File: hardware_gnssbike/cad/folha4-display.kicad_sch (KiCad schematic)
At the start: 15 parts, among them J401 Hirose FH12-10S-0.5SH(55), J402 HCTL HC-FPC-05-10-5RLTAG, Q401 DMG1012T-7

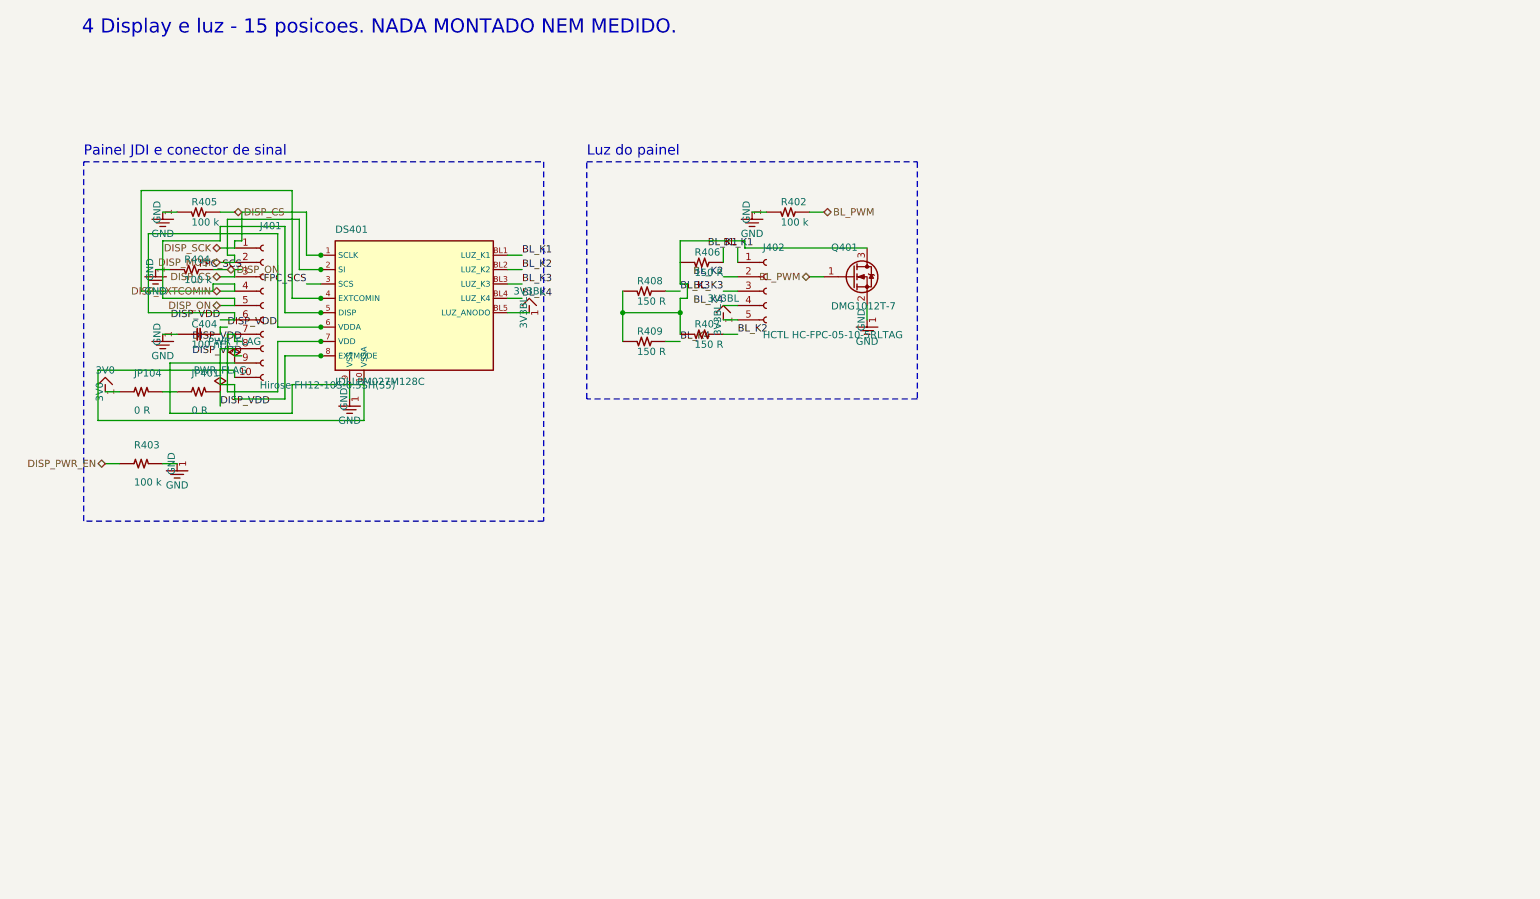
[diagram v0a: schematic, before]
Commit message: feat(hardware): spread the schematic so references, values and labels stay apart
The owner asked for the block-drawn schematic to be readable: designators
and labels were printing over each other. Power symbols now hide the pin
number and name (each printed a "1" and the rail's name twice) and point
away from their pin, lying along the line of a side pin with the name on
that line; the decoupling shelf is a row of stood-up capacitors per rail
with one wire along the tops and one symbol per row, test points standing
too; references and values sit to the right of a standing part and between
the neighbouring lines of a lying one, and block titles, part texts and
symbol names are obstacles for the router and for symbol and label
placement. Pull-ups and pull-downs of a labelled line stand past the label,
and off the corridor when the line goes on to another anchor; the labels'
room is reserved before the members are placed; the FPC connector is
mirrored to face the panel and aligned with it, its board-side wire
continuing from the label point, with the two nets of a pass-through pin
allowed to share cells; the two cells in front of every pin belong to its
net; DISP_VDD is drawn as a rail; blocks are packed by height and sheet 1
fits an A3.

The library symbol now always holds the base drawing and the instance
carries the rotation and mirror. The generator used to write the library
already flipped and the (mirror ...) token as well, applying the transform
twice, and the earlier "measurement" of (mirror x) was inverted by that.
Measured again on minimal files: (mirror y) swaps left for right, an
instance at 90 sends the left pin to the bottom, and KiCad transforms the
field justification along with the instance.

check_sch.py passes: the netlist equals nets.py pin by pin, no new ERC
error, no wire over a component. Eight nets are closed by labels where the
maze found no path inside the block, and the solar harvester and the left
of the gauge remain crowded; SCH_DEBUG=1 exp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
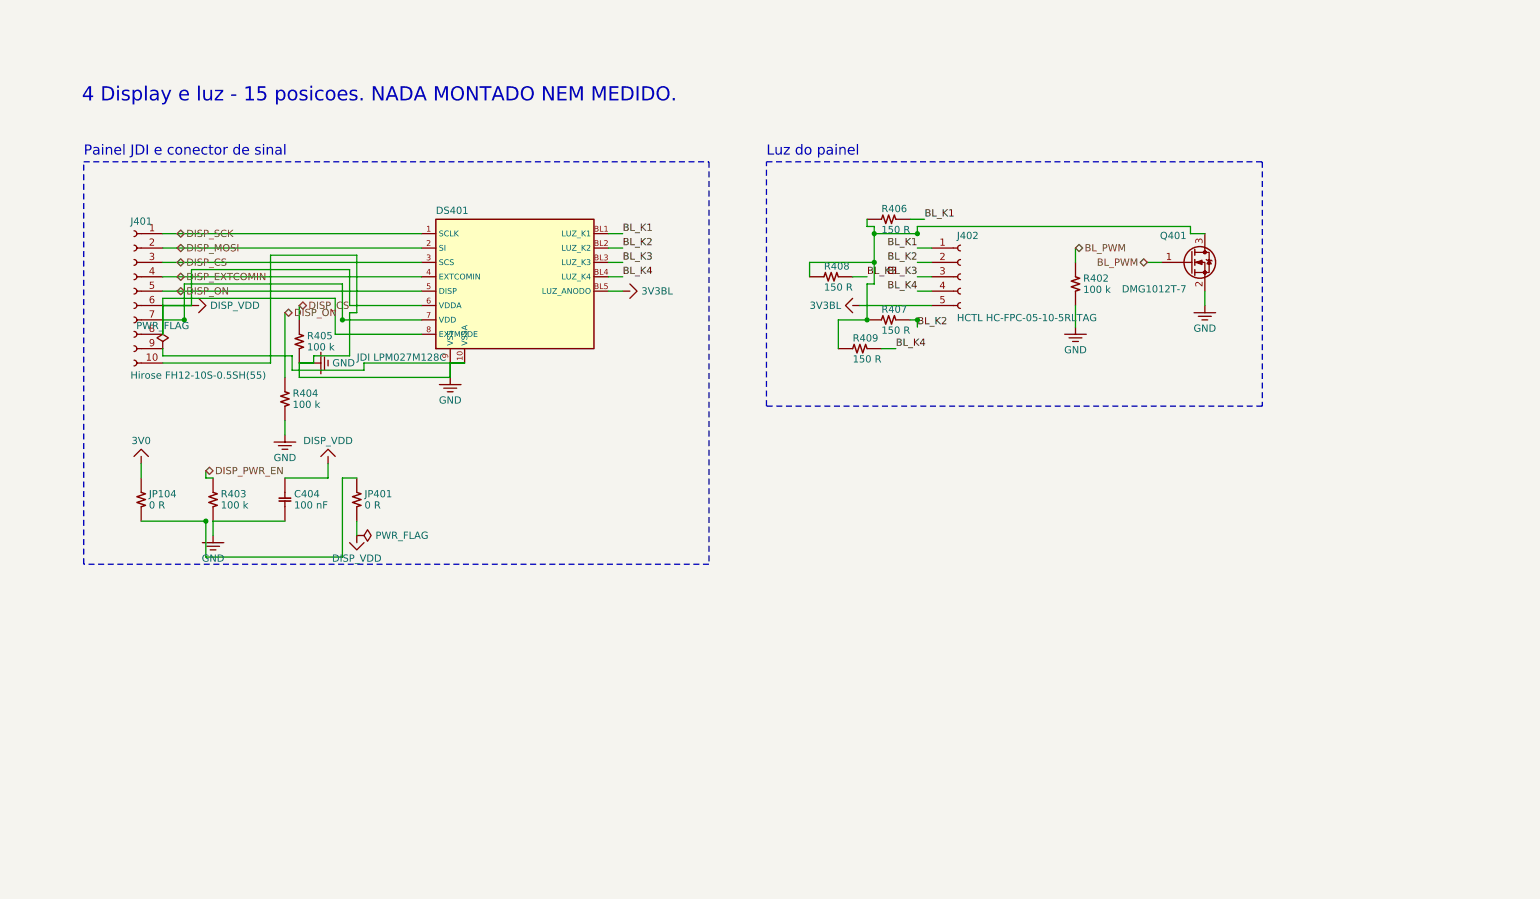
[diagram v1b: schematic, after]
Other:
- moved on the sheet: C404, DS401, J401, J402, JP104, JP401, Q401, R402, R403, R404, R405, R406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

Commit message: feat(hardware): apply the schematic review, take either display, review the case
Apply the corrections the owner approved on 2026-10-18, in the
generators: the BMP585 land from figure 29, the RGB LED land unmirrored,
the TLV7031DCKR renumbered and fed from VBAT_SYS, the common pad of
JP301 in the middle, the OPT3001 exposed pad, the Murata land for the
buck inductors, 10 uF on PVDD and 3V3BL, a 24 V TVS on VBUS, the flash
on 3V0, pin-1 marks, the charge LEDs in the key row, the TVS next to
their connectors, the USB-C on the maker's edge line, the Same Sky
buzzer in place of the last-time-buy Murata, and an LCSC code on every
fitted part.

The board takes the JDI or the Sharp on one dual-contact Molex 503480:
JP401 picks 3V0 or 5V0, and a TPS610997 boost feeds the Sharp. A second
blind check found the connector drawn backwards (the tail enters on the
nail side); the land, the circuit order and the boost placement follow
the drawings now.

The router finds its way further: unique UUIDs per footprint, so the
DRC names the right pads; the chip antenna's own nets inside its
keep-out; JP301 turned so the two RF lines do not cross; ground vias
outside the dense chips, bent and geometrically checked ground stubs,
and a pass with the power rails first. The DRC reports no error; 60
items are still unconnected.

The case is reviewed part by part (hardware_gnssbike/12): the solar
module pockets follow the datasheet's +-0.3 mm (the case grows to 64 mm),
the keys stop 0.15 mm under the membrane, and the light sensor gets a
sealed window. The sealing of the USB-C, the floor holes and the lid
seam is left to the owner. The documents follow parts.py.

Nothing is fabricated, and the routing is still open.
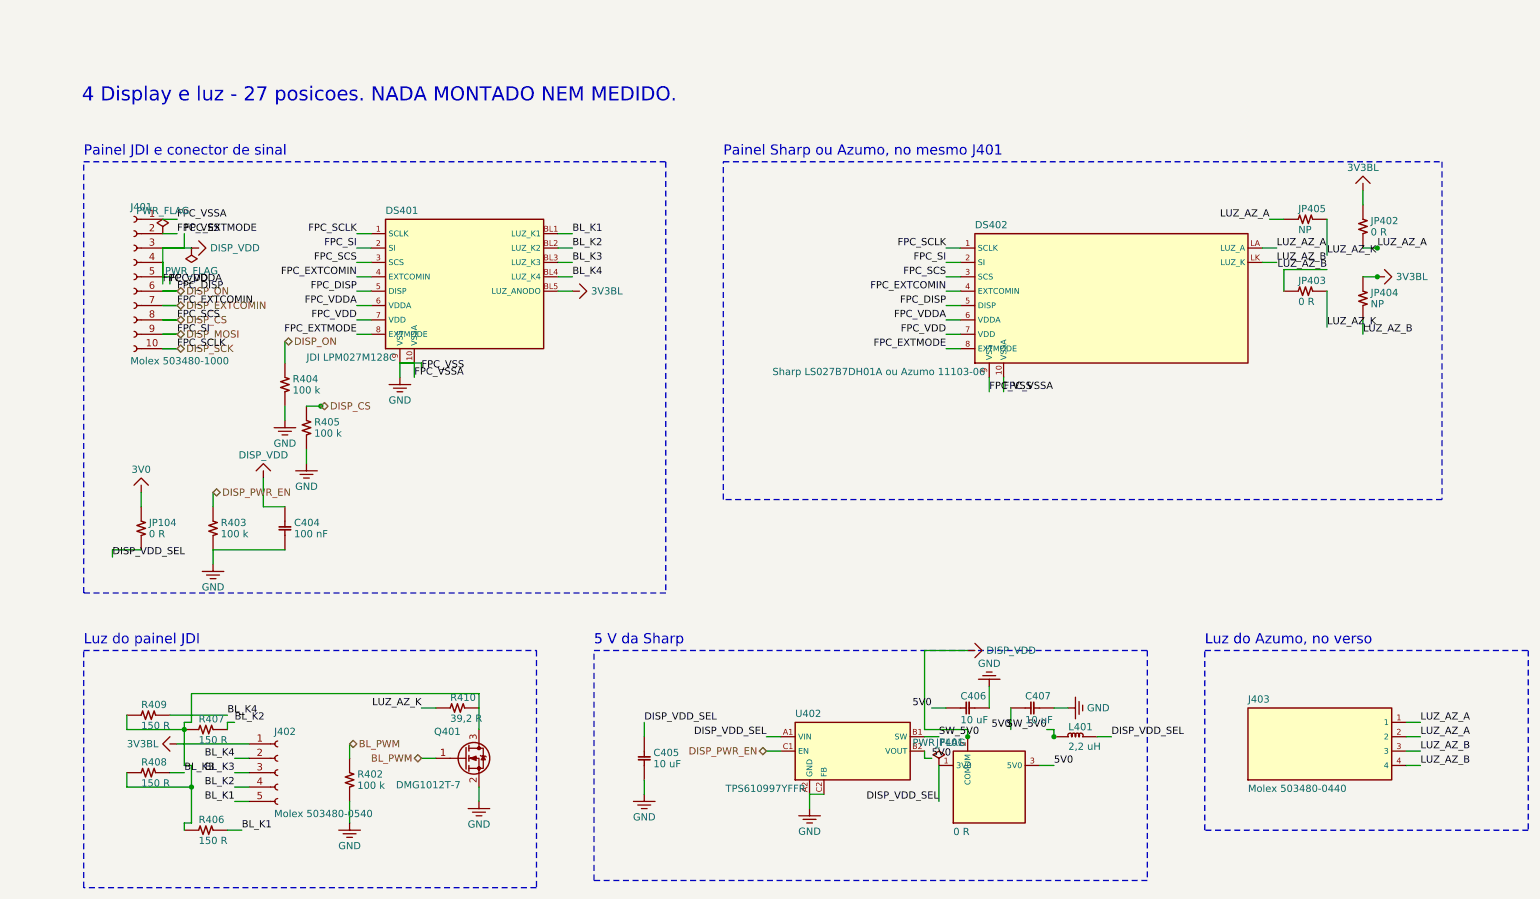
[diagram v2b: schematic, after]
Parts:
- added C405: 10 uF, Capacitor_SMD:C_0603_1608Metric, symbol gnssbike:C405
- added C406: 10 uF, Capacitor_SMD:C_0603_1608Metric, symbol gnssbike:C406
- added C407: 10 uF, Capacitor_SMD:C_0603_1608Metric, symbol gnssbike:C407
- added DS402: Sharp LS027B7DH01A ou Azumo 11103-06, symbol gnssbike:DS402
- added J403: Molex 503480-0440, gnssbike:Molex_503480-0440_1x04_P0.50mm, symbol gnssbike:J403
- added JP402: 0 R, Resistor_SMD:R_0402_1005Metric, symbol gnssbike:JP402
- added JP403: 0 R, Resistor_SMD:R_0402_1005Metric, symbol gnssbike:JP403
- added JP404: NP, Resistor_SMD:R_0402_1005Metric, symbol gnssbike:JP404
- added JP405: NP, Resistor_SMD:R_0402_1005Metric, symbol gnssbike:JP405
- added L401: 2,2 uH, Inductor_SMD:L_Murata_DFE201610P, symbol gnssbike:L401
- added R410: 39,2 R, Resistor_SMD:R_0402_1005Metric, symbol gnssbike:R410
- added U402: TPS610997YFFR, Package_BGA:Texas_DSBGA-6_0.855x1.255mm_Layout2x3_P0.4mm_LevelB, symbol gnssbike:U402
- J401: value Hirose FH12-10S-0.5SH(55) -> Molex 503480-1000; footprint Connector_FFC-FPC:Hirose_FH12-10S-0.5SH_1x10-1MP_P0.50mm_Horizontal -> gnssbike:Molex_503480-1000_1x10_P0.50mm
- J402: value HCTL HC-FPC-05-10-5RLTAG -> Molex 503480-0540; footprint gnssbike:HC-FPC-05-10-5RLTAG -> gnssbike:Molex_503480-0540_1x05_P0.50mm
- JP401: footprint Resistor_SMD:R_0402_1005Metric -> gnssbike:JumperRF_3x0402
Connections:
- net 3V3BL: now also J402.1 (Pin_1), JP402.1, JP404.1; no longer J402.5 (Pin_5)
- net BL_K1: now also J402.5 (Pin_5); no longer J402.1 (Pin_1)
- net BL_K2: now also J402.4 (Pin_4); no longer J402.2 (Pin_2)
- net BL_K4: now also J402.2 (Pin_2); no longer J402.4 (Pin_4)
- net DISP_CS: now also J401.8 (Pin_8), DS402.3 (SCS); no longer J401.3 (Pin_3)
- net DISP_EXTCOMIN: now also J401.7 (Pin_7), DS402.4 (EXTCOMIN); no longer J401.4 (Pin_4)
- net DISP_MOSI: now also J401.9 (Pin_9), DS402.2 (SI); no longer J401.2 (Pin_2)
- net DISP_ON: now also J401.6 (Pin_6), DS402.5 (DISP); no longer J401.5 (Pin_5)
- net DISP_PWR_EN: now also U402.C1 (EN)
- net DISP_SCK: now also J401.10 (Pin_10), DS402.1 (SCLK); no longer J401.1 (Pin_1)
- net DISP_VDD: now also J401.3 (Pin_3), J401.4 (Pin_4), J401.5 (Pin_5), DS402.6 (VDDA), DS402.7 (VDD), DS402.8 (EXTMODE); no longer J401.6 (Pin_6), J401.7 (Pin_7), J401.8 (Pin_8)
- net GND: now also J401.1 (Pin_1), J401.2 (Pin_2), C405.2, C406.2, C407.2, DS402.10 (VSSA), DS402.9 (VSS), U402.A2 (GND), U402.C2 (FB); no longer J401.10 (Pin_10), J401.9 (Pin_9)
- net at Q401.3 (D), R406.2, R407.2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: now also R410.2
- net DISP_VDD_SEL: now reaches JP104.2, JP401.1 (3V0)
- net DISP_VDD_SEL: now also C405.1, L401.1, U402.A1 (VIN)
- new net 5V0: C406.1, C407.1, JP401.3 (5V0), U402.B2 (VOUT)
- new net LUZ_AZ_A: DS402.LA (LUZ_A), J403.1, J403.2, JP402.2, JP405.1
- new net LUZ_AZ_B: DS402.LK (LUZ_K), J403.3, J403.4, JP403.1, JP404.2
- new net LUZ_AZ_K: JP403.2, JP405.2, R410.1
- new net SW_5V0: L401.2, U402.B1 (SW)
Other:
- note added: "4 Display e luz - 27 posicoes. NADA MONTADO NEM MEDIDO."
- note added: "5 V da Sharp"
- note added: "Luz do Azumo, no verso"
- note added: "Luz do painel JDI"
- note added: "Painel Sharp ou Azumo, no mesmo J401"
- note removed: "4 Display e luz - 15 posicoes. NADA MONTADO NEM MEDIDO."
- note removed: "Luz do painel"
- moved on the sheet: C404, DS401, J401, J402, JP104, Q401, R402, R403, R404, R405, R406, R407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
